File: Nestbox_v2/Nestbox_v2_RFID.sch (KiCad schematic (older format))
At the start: 10 parts, among them U401 MLX90109

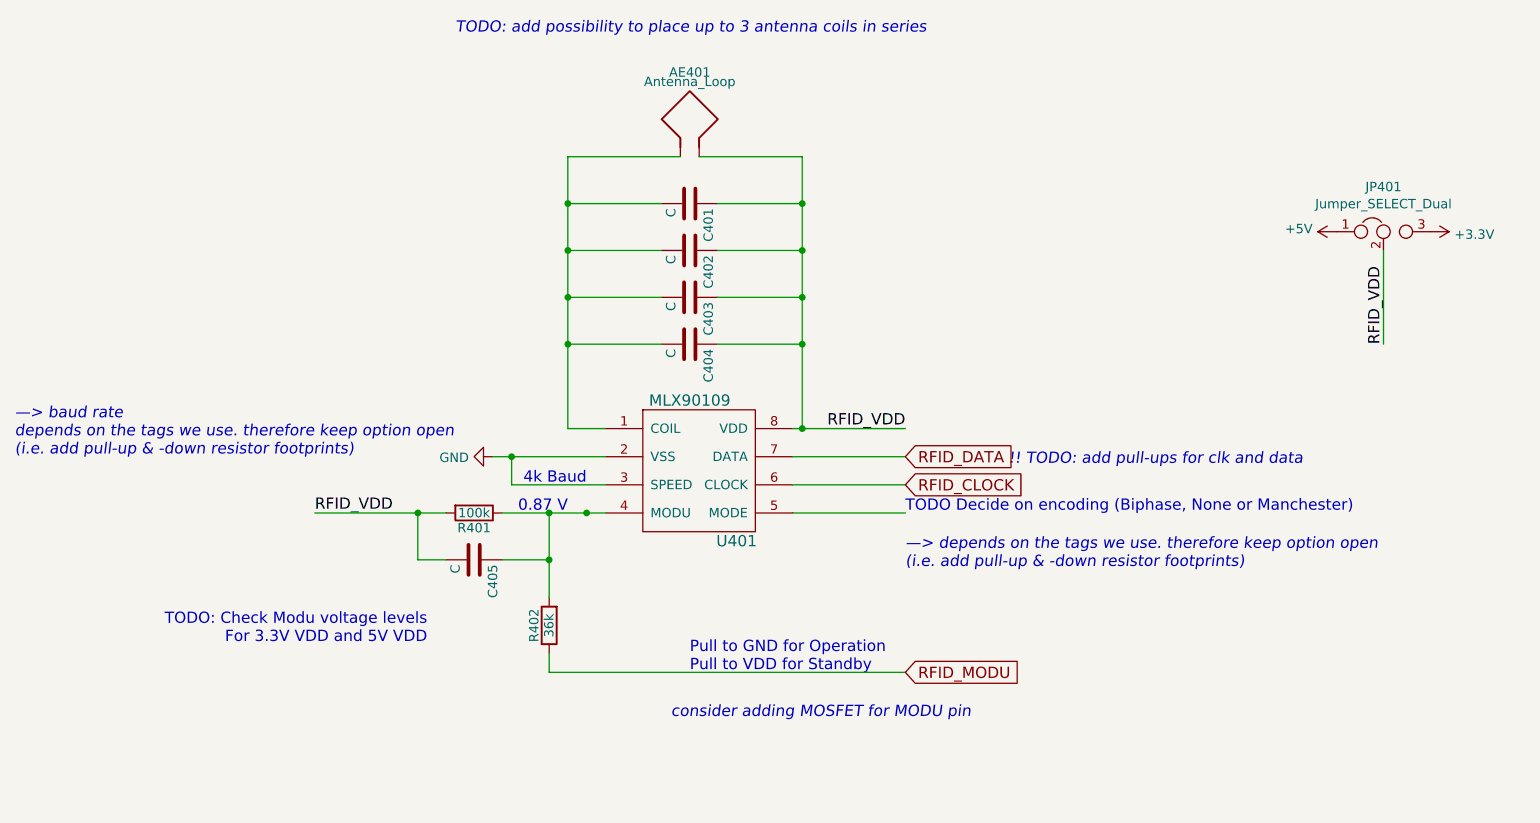
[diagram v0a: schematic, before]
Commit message: Adds Pull Up/Down Res to RFID MODE and SPEED
As per comment from Raffael, added pull up and pull down to MODE and
SPEED pins of the RFID part. This allows to later on decided on the
encoding and the baud rate.
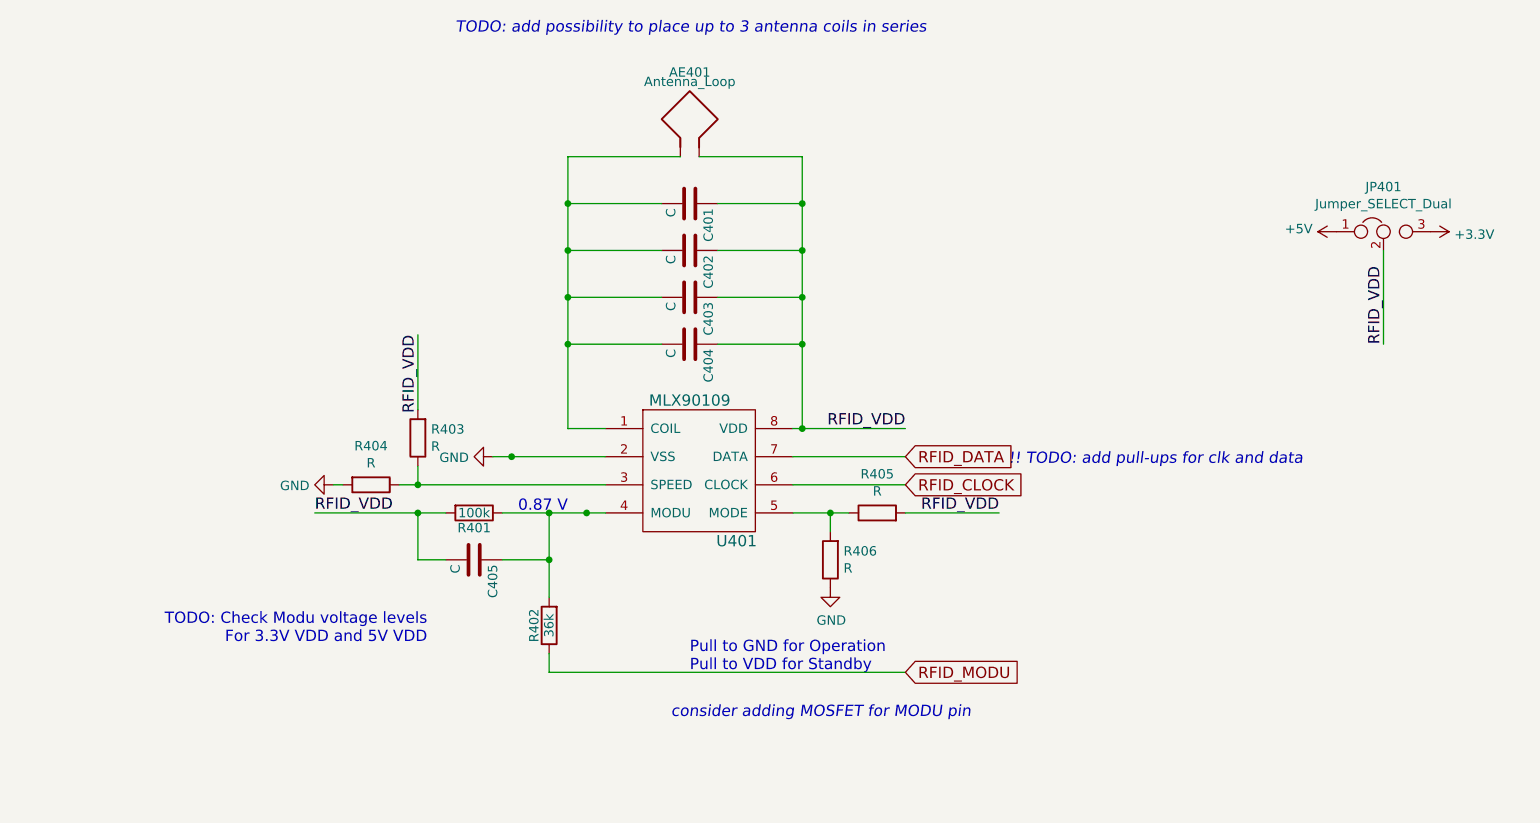
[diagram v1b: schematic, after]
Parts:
- added R403, R404, R405, R406: R, symbol R
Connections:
- net GND: now also R404.2, R406.1; no longer U401.3 (SPEED)
- net RFID_VDD: now also R403.2, R405.2
- net at U401.5 (MODE): now also R405.1, R406.2
- new net: R403.1, R404.1, U401.3 (SPEED)
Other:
- note removed: "4k Baud"
- note removed: "TODO Decide on encoding (Biphase, None or Manchester)"
- note removed: "—> baud rate \ndepends on the tags we use. therefore keep option open \n(i.e. add pull-up & -down resistor footprints)"
- note removed: "—> depends on the tags we use. therefore keep option open \n(i.e. add pull-up & -down resistor footprints)"
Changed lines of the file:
@@
 	5800 3800 6400 3800
-Wire Wire Line
-	5800 3950 6400 3950
 Wire Wire Line
 	4200 3650 4800 3650
@@
 RFID_VDD
 Wire Wire Line
-	4800 3800 4300 3800
+	3700 3800 4800 3800
 $Comp
 L C C404
@@
 Text GLabel 6400 3800 2    60   Input ~ 0
 RFID_CLOCK
-Wire Wire Line
-	4300 3800 4300 3650
 Connection ~ 4300 3650
-Text Notes 4700 3800 2    60   ~ 0
-4k Baud
 Wire Wire Line
 	4500 4800 6400 4800
@@
 Text Notes 5250 4800 0    60   ~ 0
 Pull to GND for Operation\nPull to VDD for Standby\n
-Text Notes 6400 3950 0    60   ~ 0
-TODO Decide on encoding (Biphase, None or Manchester)
 Text Notes 4600 3950 2    60   ~ 0
 0.87 V
@@
 Text Notes 5150 5050 0    60   Italic 0
 consider adding MOSFET for MODU pin\n
-Text Notes 6400 4250 0    60   Italic 0
-—> depends on the tags we use. therefore keep option open \n(i.e. add pull-up & -down resistor footprints)
-Text Notes 1650 3650 0    60   Italic 0
-—> baud rate \ndepends on the tags we use. therefore keep option open \n(i.e. add pull-up & -down resistor footprints)
 Text Notes 4000 1400 0    60   Italic 0
 TODO: add possibility to place up to 3 antenna coils in series
 Text Notes 6950 3700 0    60   Italic 0
 !! TODO: add pull-ups for clk and data\n
+$Comp
+L R R404
+U 1 1 5A0B4046
+P 3550 3800
+F 0 "R404" V 3343 3800 50  0000 C CNN
+F 1 "R" V 3434 3800 50  0000 C CNN
+F 2 "" V 3480 3800 50  0001 C CNN
+F 3 "" H 3550 3800 50  0001 C CNN
+	1    3550 3800
+	0    1    1    0
+$EndComp
+$Comp
+L R R403
+U 1 1 5A0B40C6
+P 3800 3550
+F 0 "R403" H 3730 3504 50  0000 R CNN
+F 1 "R" H 3730 3595 50  0000 R CNN
+F 2 "" V 3730 3550 50  0001 C CNN
+F 3 "" H 3800 3550 50  0001 C CNN
+	1    3800 3550
+	-1   0    0    1
+$EndComp
+Wire Wire Line
+	3800 3400 3800 3000
+Text Label 3800 3000 3    60   ~ 0
+RFID_VDD
+Wire Wire Line
+	3800 3700 3800 3800
+Connection ~ 3800 3800
+$Comp
+L GND #PWR0404
+U 1 1 5A0B428A
+P 3350 3800
+F 0 "#PWR0404" H 3350 3550 50  0001 C CNN
+F 1 "GND" V 3355 3672 50  0000 R CNN
+F 2 "" H 3350 3800 50  0001 C CNN
+F 3 "" H 3350 3800 50  0001 C CNN
+	1    3350 3800
+	0    1    1    0
+$EndComp
+Wire Wire Line
+	3400 3800 3350 3800
+$Comp
+L R R406
+U 1 1 5A0B4313
+P 6000 4200
+F 0 "R406" H 5930 4154 50  0000 R CNN
+F 1 "R" H 5930 4245 50  0000 R CNN
+F 2 "" V 5930 4200 50  0001 C CNN
+F 3 "" H 6000 4200 50  0001 C CNN
+	1    6000 4200
+	-1   0    0    1
+$EndComp
+$Comp
+L R R405
+U 1 1 5A0B439E
+P 6250 3950
+F 0 "R405" V 6457 3950 50  0000 C CNN
+F 1 "R" V 6366 3950 50  0000 C CNN
+F 2 "" V 6180 3950 50  0001 C CNN
+F 3 "" H 6250 3950 50  0001 C CNN
+	1    6250 3950
+	0    -1   -1   0
+$EndComp
+Wire Wire Line
+	5800 3950 6100 3950
+Wire Wire Line
+	6000 4050 6000 3950
+Connection ~ 6000 3950
+$Comp
+L GND #PWR0405
+U 1 1 5A0B45F2
+P 6000 4350
+F 0 "#PWR0405" H 6000 4100 50  0001 C CNN
+F 1 "GND" H 6005 4177 50  0000 C CNN
+F 2 "" H 6000 4350 50  0001 C CNN
+F 3 "" H 6000 4350 50  0001 C CNN
+	1    6000 4350
+	1    0    0    -1
+$EndComp
+Wire Wire Line
+	6400 3950 6900 3950
+Text Label 6900 3950 2    60   ~ 0
+RFID_VDD
 $EndSCHEMATC

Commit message: Adds a N-Mosfet to the RFID-Modu pin
This way we are independant of the chosen RFID power supply voltage.
Name of RFID_MODU signal was changed to RFID_MODU_N to indicate inversed
logic level due to the N-Mosfet.
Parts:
- added Q?: Q_NMOS_DGS, symbol Q_NMOS_DGS
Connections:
- net GND: now also Q?.3 (S)
- net RFID_MODU: no longer names the net of R402.1
- net RFID_MODU: now also Q?.1 (D)
- new net RFID_MODU_N: Q?.2 (G)
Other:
- note removed: "TODO: Check Modu voltage levels\nFor 3.3V VDD and 5V VDD"
- note removed: "consider adding MOSFET for MODU pin\n"
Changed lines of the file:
@@
 RFID_CLOCK
 Connection ~ 4300 3650
-Wire Wire Line
-	4500 4800 6400 4800
 Connection ~ 4700 3950
-Text GLabel 6400 4800 2    60   Input ~ 0
-RFID_MODU
-Text Notes 5250 4800 0    60   ~ 0
+Text Notes 4500 4800 0    60   ~ 0
 Pull to GND for Operation\nPull to VDD for Standby\n
 Text Notes 4600 3950 2    60   ~ 0
@@
 	0    -1   -1   0
 $EndComp
-Text Notes 3850 4650 2    60   ~ 0
-TODO: Check Modu voltage levels\nFor 3.3V VDD and 5V VDD
 $Comp
 L GND #PWR0403
@@
 	0    1    1    0
 $EndComp
-Text Notes 5150 5050 0    60   Italic 0
-consider adding MOSFET for MODU pin\n
 Text Notes 4000 1400 0    60   Italic 0
 TODO: add possibility to place up to 3 antenna coils in series
@@
 Text Label 6900 3950 2    60   ~ 0
 RFID_VDD
+$Comp
+L Q_NMOS_DGS Q?
+U 1 1 5A0DB463
+P 4400 5000
+F 0 "Q?" H 4605 5046 50  0000 L CNN
+F 1 "Q_NMOS_DGS" H 4605 4955 50  0000 L CNN
+F 2 "" H 4600 5100 50  0001 C CNN
+F 3 "" H 4400 5000 50  0001 C CNN
+	1    4400 5000
+	1    0    0    -1
+$EndComp
+$Comp
+L GND #PWR?
+U 1 1 5A0DB4D4
+P 4500 5300
+F 0 "#PWR?" H 4500 5050 50  0001 C CNN
+F 1 "GND" H 4505 5127 50  0000 C CNN
+F 2 "" H 4500 5300 50  0001 C CNN
+F 3 "" H 4500 5300 50  0001 C CNN
+	1    4500 5300
+	1    0    0    -1
+$EndComp
+Wire Wire Line
+	4500 5200 4500 5300
+Text GLabel 4100 5000 0    60   Input ~ 0
+RFID_MODU_N
+Wire Wire Line
+	4100 5000 4200 5000
 $EndSCHEMATC
